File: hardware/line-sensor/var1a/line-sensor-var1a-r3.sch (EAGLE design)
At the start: 141 parts, among them IC1 GP2S60, IC10 GP2S60, IC11 GP2S60, IC12 GP2S60, IC13 GP2S60, IC14 GP2S60, IC15 GP2S60, IC16 GP2S60, IC17 GP2S60, IC18 GP2S60, IC19 GP2S60, IC2 GP2S60, IC20 GP2S60, IC21 GP2S60, IC22 GP2S60, IC23 GP2S60, IC24 GP2S60, IC25 GP2S60, IC26 GP2S60, IC27 GP2S60, IC28 STM32L151VE, IC3 GP2S60, IC32 LM5165YDRCR, IC4 GP2S60, IC5 GP2S60, IC6 GP2S60, IC7 GP2S60, IC8 GP2S60, IC9 GP2S60, J1 MOLEX-502382-06XX, J2 MOLEX-53261-0771, J3 MOLEX-502382-02XX, Y1 CRYSTALKYOCERA-CX3225GB24000D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, Y2 CRYSTALNDK-NX3215SA

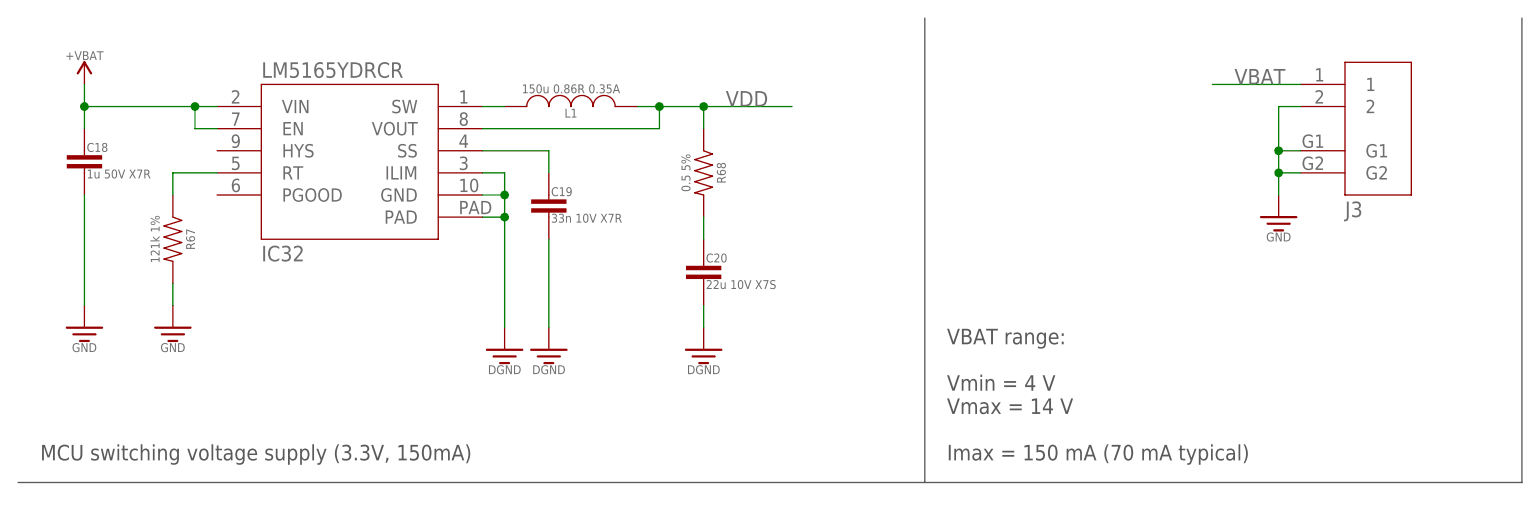
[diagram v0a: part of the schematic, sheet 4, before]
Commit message: finished 3rd revision of line sensor
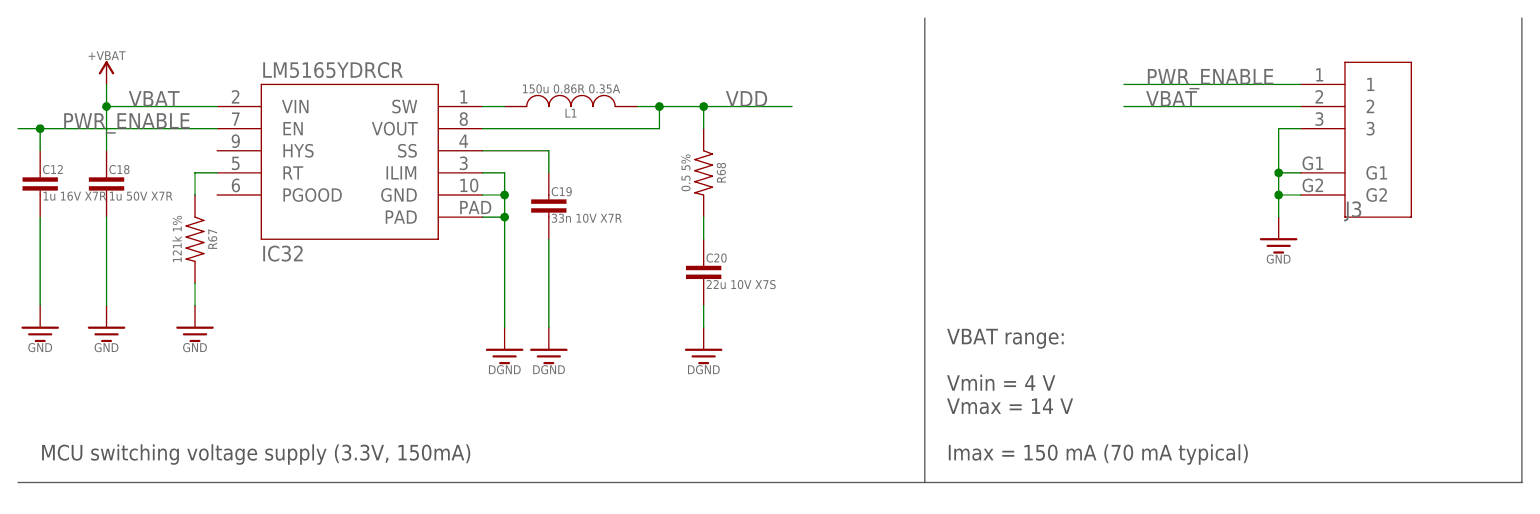
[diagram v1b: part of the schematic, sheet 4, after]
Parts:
- added C12: 1u 16V X7R, passives:CAPACITOR0603
- J3: value MOLEX-502382-02XX -> MOLEX-502382-03XX; device connectors:MOLEX-502382-02XX -> connectors:MOLEX-502382-03XX
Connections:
- new net PWR_ENABLE: C12.1, IC32.EN, J3.1
- net GND: now also C12.2, J3.3; no longer J3.2
- net VBAT: now also J3.2; no longer IC32.EN, J3.1
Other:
- note added: "Revision 3 changes: - removed I2C - removed USART2 - moved communication traces and jumpers away from L1 - added quarz crystals (24 MHz, 32.768 kHz) to improve clocks precision - added wakup signal - bank B ADC is now on last sensor - moved decoupling capacitors closer to MCU - added power regulator on/off signal"
- note removed: "Revision 3 changes: - removed I2C - removed USART2 - moved communication traces and jumpers away from L1 - added quarz crystals (24 MHz, 32.768 kHz) to improve clocks precision - added wakup signal - bank B ADC is now on last sensor - moved decoupling capacitors closer to MCU"
- moved on the sheet: C18, R67
